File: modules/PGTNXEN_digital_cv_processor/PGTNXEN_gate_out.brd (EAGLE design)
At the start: 52 x 38.1 mm, 47 parts, among them IC1 74HC595N, IC2 TL074P, IC3 TL074P

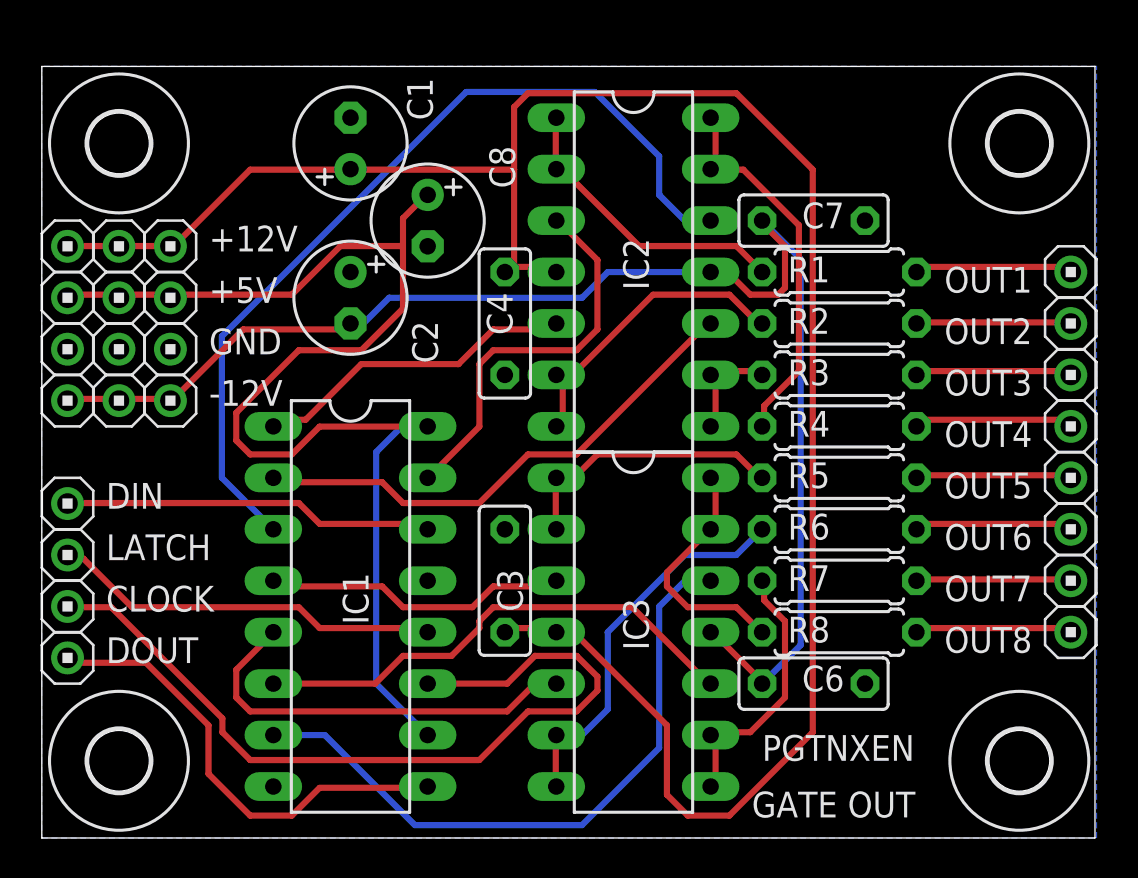
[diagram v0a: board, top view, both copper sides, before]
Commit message: PGTN020 - ADSR Envelope with VCA
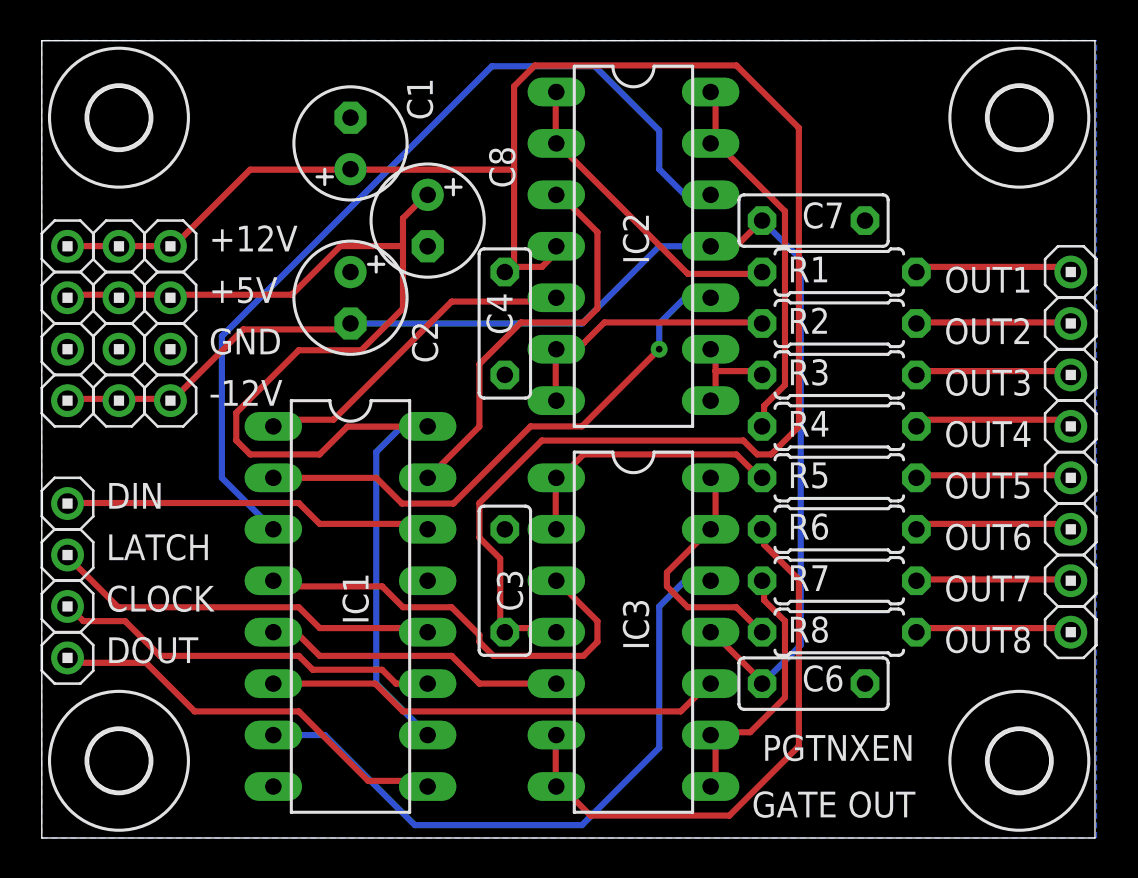
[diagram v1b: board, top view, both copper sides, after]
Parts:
- moved IC2 1.27 mm to (29.2, 55.9)
- moved U$3 1.27 mm to (48.3, 62.2)
- moved U$4 1.27 mm to (3.81, 62.2)
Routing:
- net N$3: track 41.2 -> 19.3 mm
- net N$24: track 19.1 -> 28.0 mm
- net N$17: track 102.3 -> 94.5 mm
- net N$8: track 15.2 -> 21.9 mm
- net N$9: track 20.6 -> 15.0 mm
- net N$18: track 70.8 -> 66.3 mm
- net N$12: track 23.0 -> 20.5 mm
- net N$15: track 15.7 -> 13.3 mm
- net N$10: track 24.9 -> 22.7 mm
- net N$6: track 25.8 -> 27.1 mm, vias 0 -> 1
- net N$1: track 19.5 -> 20.2 mm
- net N$13: track 14.8 -> 15.4 mm
- net N$7: track 43.5 -> 44.0 mm
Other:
- board size 52 x 38.1 mm -> 52 x 39.4 mm
